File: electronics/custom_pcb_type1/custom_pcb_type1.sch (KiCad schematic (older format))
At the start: 24 parts, among them J1 BELT_CONN_1, J2 BELT_CONN_2, J3 SEN0140, Q1 2N2222, Q2 2N2222, Q3 2N2222, Q4 2N2222, Q5 2N2222, Q6 2N2222, SW1 RST_SW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

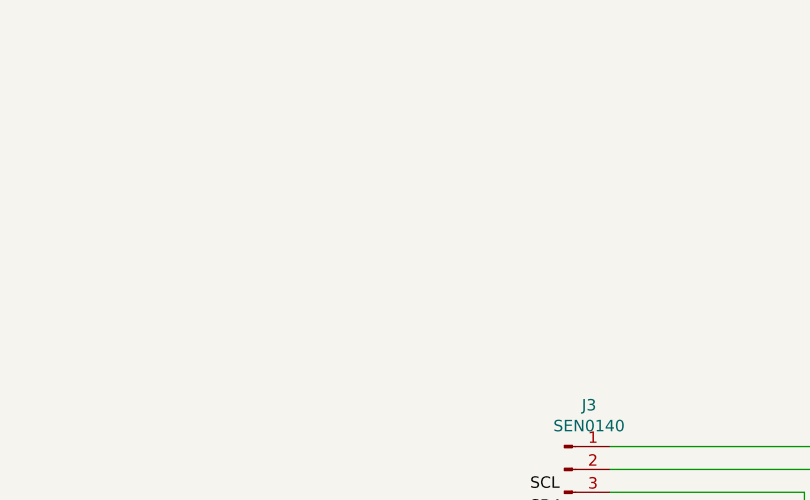
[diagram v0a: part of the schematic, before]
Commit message: Added USB connector
I'm pulling power from a secondary USB port on my prototype board and I plan to do the same here. The +5V from the USB port is used directly by everything and is passed to the atmega through its usb port.
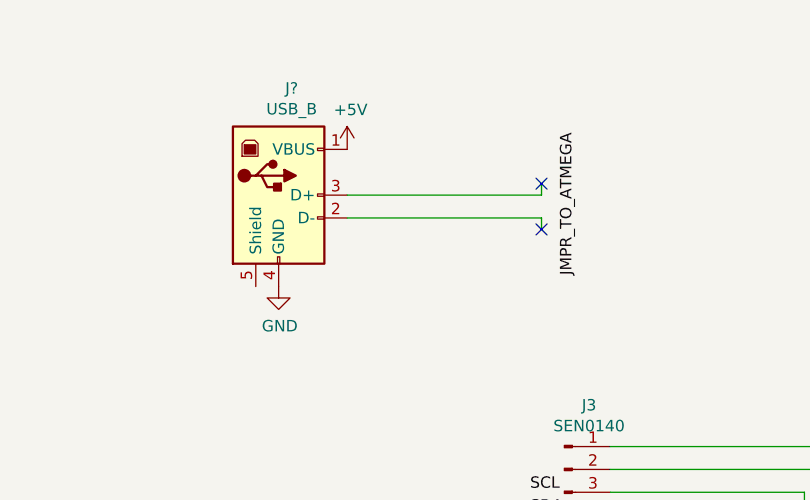
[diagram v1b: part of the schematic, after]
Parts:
- added J?: USB_B, symbol Connector:USB_B
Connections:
- net +5V: now also J?.1 (VBUS)
- net GND: now also J?.4 (GND)
- no-connect marks 0 -> 2
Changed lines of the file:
@@
 Wire Wire Line
 	5250 3150 5250 3600
+$Comp
+L Connector:USB_B J?
+U 1 1 609CD78C
+P 1150 1300
+F 0 "J?" H 1207 1767 50  0000 C CNN
+F 1 "USB_B" H 1207 1676 50  0000 C CNN
+F 2 "" H 1300 1250 50  0001 C CNN
+F 3 " ~" H 1300 1250 50  0001 C CNN
+	1    1150 1300
+	1    0    0    -1
+$EndComp
+$Comp
+L power:GND #PWR?
+U 1 1 609CF541
+P 1150 1700
+F 0 "#PWR?" H 1150 1450 50  0001 C CNN
+F 1 "GND" H 1155 1527 50  0000 C CNN
+F 2 "" H 1150 1700 50  0001 C CNN
+F 3 "" H 1150 1700 50  0001 C CNN
+	1    1150 1700
+	1    0    0    -1
+$EndComp
+$Comp
+L power:+5V #PWR?
+U 1 1 609D041E
+P 1450 1100
+F 0 "#PWR?" H 1450 950 50  0001 C CNN
+F 1 "+5V" H 1465 1273 50  0000 C CNN
+F 2 "" H 1450 1100 50  0001 C CNN
+F 3 "" H 1450 1100 50  0001 C CNN
+	1    1450 1100
+	1    0    0    -1
+$EndComp
+Wire Wire Line
+	2300 1300 2300 1250
+Wire Wire Line
+	1450 1300 2300 1300
+Wire Wire Line
+	1450 1400 2300 1400
+Wire Wire Line
+	2300 1400 2300 1450
+NoConn ~ 2300 1250
+NoConn ~ 2300 1450
+Text Label 2450 1650 1    50   ~ 0
+JMPR_TO_ATMEGA
 $EndSCHEMATC

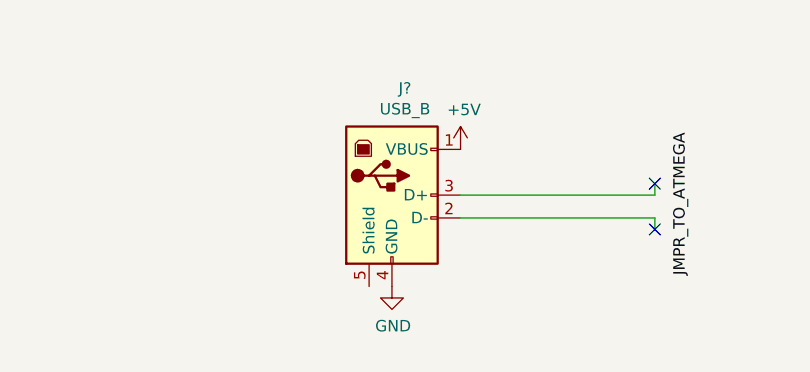
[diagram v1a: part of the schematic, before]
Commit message: Physical PCB start
Sort of got a start on the physical PCB layout. Its hard to lay things out in ways that don't overlap with other traces on a single layer. I got most of everything connected up and I think what I have left will need to be on the other side of the PCB. Will try and figure that out tomorrow.
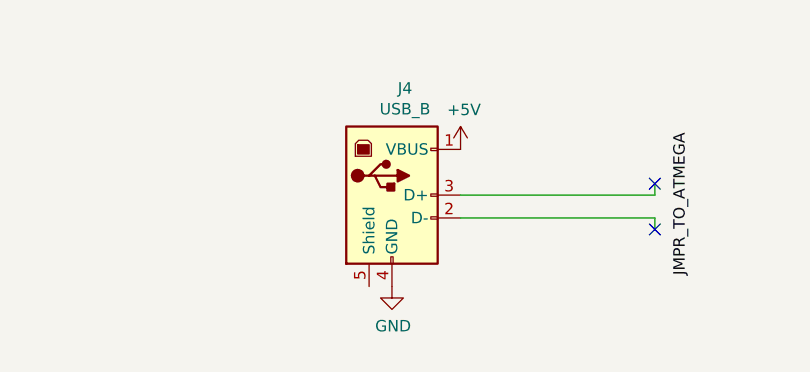
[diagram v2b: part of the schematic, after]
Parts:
- D1: footprint (none) -> LED_THT:LED_D5.0mm-4_RGB_Staggered_Pins
- J1, J2: footprint (none) -> Connector_PinHeader_2.54mm:PinHeader_2x03_P2.54mm_Horizontal
- J3: footprint (none) -> Connector_PinSocket_2.54mm:PinSocket_1x04_P2.54mm_Vertical
- J4: renamed from J?; footprint (none) -> Connector_USB:USB_B_OST_USB-B1HSxx_Horizontal
- R1, R2, R3, R4, R5, R6, R7, R8, R9: footprint (none) -> Resistor_THT:R_Axial_DIN0207_L6.3mm_D2.5mm_P10.16mm_Horizontal
- RV1, RV2, RV3: footprint (none) -> Potentiometer_THT:Potentiometer_Runtron_RM-065_Vertical
- SW1: footprint (none) -> Button_Switch_THT:SW_PUSH_6mm
- U1: footprint MODULE_MEGA_PRO_EMBED_CH340G_/_ATMEGA2560 -> MODULE_MEGA_PRO_EMBED_CH340G_:_ATMEGA2560
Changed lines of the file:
@@
 F 0 "U1" V 3204 1770 50  0000 R CNN
 F 1 "MEGA_PRO_EMBED_CH340G___ATMEGA2560" V 3295 1770 50  0000 R CNN
-F 2 "MODULE_MEGA_PRO_EMBED_CH340G_/_ATMEGA2560" H 3250 4300 50  0001 L BNN
+F 2 "MODULE_MEGA_PRO_EMBED_CH340G_:_ATMEGA2560" H 3250 4300 50  0001 L BNN
 F 3 "" H 3250 4300 50  0001 L BNN
 F 4 "" H 3250 4300 50  0001 L BNN "MAXIMUM_PACKAGE_HIEGHT"
@@
 F 0 "J2" H 10322 2424 50  0000 R CNN
 F 1 "BELT_CONN_2" H 10322 2333 50  0000 R CNN
-F 2 "" H 10350 2450 50  0001 C CNN
+F 2 "Connector_PinHeader_2.54mm:PinHeader_2x03_P2.54mm_Horizontal" H 10350 2450 50  0001 C CNN
 F 3 "~" H 10350 2450 50  0001 C CNN
 	1    10350 2450
@@
 F 0 "J1" H 10322 3624 50  0000 R CNN
 F 1 "BELT_CONN_1" H 10322 3533 50  0000 R CNN
-F 2 "" H 10350 3650 50  0001 C CNN
+F 2 "Connector_PinHeader_2.54mm:PinHeader_2x03_P2.54mm_Horizontal" H 10350 3650 50  0001 C CNN
 F 3 "~" H 10350 3650 50  0001 C CNN
 	1    10350 3650
@@
 F 0 "D1" H 1300 6497 50  0000 C CNN
 F 1 "LED_RGBC" H 1300 6406 50  0000 C CNN
-F 2 "" H 1300 5950 50  0001 C CNN
+F 2 "LED_THT:LED_D5.0mm-4_RGB_Staggered_Pins" H 1300 5950 50  0001 C CNN
 F 3 "~" H 1300 5950 50  0001 C CNN
 	1    1300 6000
@@
 F 0 "R4" V 5300 1100 50  0000 L CNN
 F 1 "1.8K" V 5400 1100 50  0000 L CNN
-F 2 "" H 5200 1150 50  0001 C CNN
+F 2 "Resistor_THT:R_Axial_DIN0207_L6.3mm_D2.5mm_P10.16mm_Horizontal" H 5200 1150 50  0001 C CNN
 F 3 "~" H 5200 1150 50  0001 C CNN
 	1    5200 1150
@@
 F 0 "R5" H 6368 1446 50  0000 L CNN
 F 1 "1.8K" H 6368 1355 50  0000 L CNN
-F 2 "" H 6300 1400 50  0001 C CNN
+F 2 "Resistor_THT:R_Axial_DIN0207_L6.3mm_D2.5mm_P10.16mm_Horizontal" H 6300 1400 50  0001 C CNN
 F 3 "~" H 6300 1400 50  0001 C CNN
 	1    6300 1400
@@
 F 0 "R6" H 7168 1446 50  0000 L CNN
 F 1 "1.8K" H 7168 1355 50  0000 L CNN
-F 2 "" H 7100 1400 50  0001 C CNN
+F 2 "Resistor_THT:R_Axial_DIN0207_L6.3mm_D2.5mm_P10.16mm_Horizontal" H 7100 1400 50  0001 C CNN
 F 3 "~" H 7100 1400 50  0001 C CNN
 	1    7100 1400
@@
 F 0 "R7" H 7968 1446 50  0000 L CNN
 F 1 "1.8K" H 7968 1355 50  0000 L CNN
-F 2 "" H 7900 1400 50  0001 C CNN
+F 2 "Resistor_THT:R_Axial_DIN0207_L6.3mm_D2.5mm_P10.16mm_Horizontal" H 7900 1400 50  0001 C CNN
 F 3 "~" H 7900 1400 50  0001 C CNN
 	1    7900 1400
@@
 F 0 "R8" H 8768 1446 50  0000 L CNN
 F 1 "1.8K" H 8768 1355 50  0000 L CNN
-F 2 "" H 8700 1400 50  0001 C CNN
+F 2 "Resistor_THT:R_Axial_DIN0207_L6.3mm_D2.5mm_P10.16mm_Horizontal" H 8700 1400 50  0001 C CNN
 F 3 "~" H 8700 1400 50  0001 C CNN
 	1    8700 1400
@@
 F 0 "R9" H 9568 1446 50  0000 L CNN
 F 1 "1.8K" H 9568 1355 50  0000 L CNN
-F 2 "" H 9500 1400 50  0001 C CNN
+F 2 "Resistor_THT:R_Axial_DIN0207_L6.3mm_D2.5mm_P10.16mm_Horizontal" H 9500 1400 50  0001 C CNN
 F 3 "~" H 9500 1400 50  0001 C CNN
 	1    9500 1400
@@
 F 0 "R1" H 1768 5546 50  0000 L CNN
 F 1 "330" H 1768 5455 50  0000 L CNN
-F 2 "" H 1700 5500 50  0001 C CNN
+F 2 "Resistor_THT:R_Axial_DIN0207_L6.3mm_D2.5mm_P10.16mm_Horizontal" H 1700 5500 50  0001 C CNN
 F 3 "~" H 1700 5500 50  0001 C CNN
 	1    1700 5500
@@
 F 0 "R2" H 2218 6096 50  0000 L CNN
 F 1 "330" H 2218 6005 50  0000 L CNN
-F 2 "" H 2150 6050 50  0001 C CNN
+F 2 "Resistor_THT:R_Axial_DIN0207_L6.3mm_D2.5mm_P10.16mm_Horizontal" H 2150 6050 50  0001 C CNN
 F 3 "~" H 2150 6050 50  0001 C CNN
 	1    2150 6050
@@
 F 0 "R3" H 2318 5296 50  0000 L CNN
 F 1 "330" H 2318 5205 50  0000 L CNN
-F 2 "" H 2250 5250 50  0001 C CNN
+F 2 "Resistor_THT:R_Axial_DIN0207_L6.3mm_D2.5mm_P10.16mm_Horizontal" H 2250 5250 50  0001 C CNN
 F 3 "~" H 2250 5250 50  0001 C CNN
 	1    2250 5250
@@
 F 0 "RV1" H 1833 7146 50  0000 R CNN
 F 1 "10K" H 1833 7055 50  0000 R CNN
-F 2 "" H 1900 7100 50  0001 C CNN
+F 2 "Potentiometer_THT:Potentiometer_Runtron_RM-065_Vertical" H 1900 7100 50  0001 C CNN
 F 3 "~" H 1900 7100 50  0001 C CNN
 	1    1900 7100
@@
 F 0 "RV2" H 2833 7146 50  0000 R CNN
 F 1 "10K" H 2833 7055 50  0000 R CNN
-F 2 "" H 2900 7100 50  0001 C CNN
+F 2 "Potentiometer_THT:Potentiometer_Runtron_RM-065_Vertical" H 2900 7100 50  0001 C CNN
 F 3 "~" H 2900 7100 50  0001 C CNN
 	1    2900 7100
@@
 F 0 "RV3" H 4033 7146 50  0000 R CNN
 F 1 "10K" H 4033 7055 50  0000 R CNN
-F 2 "" H 4100 7100 50  0001 C CNN
+F 2 "Potentiometer_THT:Potentiometer_Runtron_RM-065_Vertical" H 4100 7100 50  0001 C CNN
 F 3 "~" H 4100 7100 50  0001 C CNN
 	1    4100 7100
@@
 F 0 "J3" H 2508 2781 50  0000 C CNN
 F 1 "SEN0140" H 2508 2690 50  0000 C CNN
-F 2 "" H 2400 2500 50  0001 C CNN
+F 2 "Connector_PinSocket_2.54mm:PinSocket_1x04_P2.54mm_Vertical" H 2400 2500 50  0001 C CNN
 F 3 "~" H 2400 2500 50  0001 C CNN
 	1    2400 2500
@@
 F 0 "SW1" V 5296 2902 50  0000 R CNN
 F 1 "RST_SW" V 5205 2902 50  0000 R CNN
-F 2 "" H 5250 3150 50  0001 C CNN
+F 2 "Button_Switch_THT:SW_PUSH_6mm" H 5250 3150 50  0001 C CNN
 F 3 "http://www.apem.com/int/index.php?controller=attachment&id_attachment=488" H 5250 3150 50  0001 C CNN
 	1    5250 2950
@@
 	5250 3150 5250 3600
 $Comp
-L Connector:USB_B J?
+L Connector:USB_B J4
 U 1 1 609CD78C
 P 1150 1300
-F 0 "J?" H 1207 1767 50  0000 C CNN
+F 0 "J4" H 1207 1767 50  0000 C CNN
 F 1 "USB_B" H 1207 1676 50  0000 C CNN
-F 2 "" H 1300 1250 50  0001 C CNN
+F 2 "Connector_USB:USB_B_OST_USB-B1HSxx_Horizontal" H 1300 1250 50  0001 C CNN
 F 3 " ~" H 1300 1250 50  0001 C CNN
 	1    1150 1300
@@
 $EndComp
 $Comp
-L power:GND #PWR?
+L power:GND #PWR0111
 U 1 1 609CF541
 P 1150 1700
-F 0 "#PWR?" H 1150 1450 50  0001 C CNN
+F 0 "#PWR0111" H 1150 1450 50  0001 C CNN
 F 1 "GND" H 1155 1527 50  0000 C CNN
 F 2 "" H 1150 1700 50  0001 C CNN
@@
 $EndComp
 $Comp
-L power:+5V #PWR?
+L power:+5V #PWR0112
 U 1 1 609D041E
 P 1450 1100
-F 0 "#PWR?" H 1450 950 50  0001 C CNN
+F 0 "#PWR0112" H 1450 950 50  0001 C CNN
 F 1 "+5V" H 1465 1273 50  0000 C CNN
 F 2 "" H 1450 1100 50  0001 C CNN

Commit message: Better PCB routing
Before I started doing the back side routing I decided to try rerouting things for more traces on the top layer. I ended up changing the pinout to use even numbered pins 2-12 backwards (i.e. first motor is on pin 12, last motor on pin 2). That made routing SO much easier and I probably should have done that first. Now I think I'm down to just power and ground traces which I will have to do on the back for the most part. I know generally you're supposed to put data and power on the top layer and ground traces on the bottom but in this case just finishing it is all I want. Our bottom layer will be carefully placed ground and power traces unless we can finagle more room out of the top.
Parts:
- removed SW1: RST_SW, Button_Switch_THT:SW_PUSH_6mm, symbol Switch:SW_MEC_5G
- added SW1: RST_SW, Button_Switch_THT:SW_PUSH_6mm, symbol Switch:SW_Push
- D1: footprint LED_THT:LED_D5.0mm-4_RGB_Staggered_Pins -> LED_THT:LED_D5.0mm-4_RGB; symbol Device:LED_RGBC -> Device:LED_RGBC_GND2
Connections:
- net +5V: no longer J3.1 (Pin_1)
- net GND: now also D1.2 (K), SW1.1; no longer D1.4 (K), J3.2 (Pin_2)
- net at U1.5V_1 (5V), U1.5V_2 (5V), U1.5V_3 (5V): now also J3.1 (Pin_1)
- net at U1.D10: now also R5.2; no longer R9.2
- net at U1.D12: now also R4.2
- net at U1.D2: now also R9.2
- net at U1.D4: now also R8.2
- net at U1.D5: no longer R4.2
- net at U1.D6: now also R7.2; no longer R5.2
- net at U1.D7: no longer R6.2
- net at U1.D8: now also R6.2; no longer R7.2
- net at U1.D9: no longer R8.2
- net at U1.GND_1 (GND), U1.GND_2 (GND), U1.GND_3 (GND): now also J3.2 (Pin_2)
- net at U1.RST: now also SW1.2
- net at R1.2: now also D1.3 (GA); no longer D1.2 (GA)
- net at R2.2: now also D1.4 (BA); no longer D1.3 (BA)
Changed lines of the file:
@@
 	5500 1150 5300 1150
 Wire Wire Line
-	4250 1150 4250 3600
-Wire Wire Line
-	4150 5000 4150 5650
-Wire Wire Line
-	4150 5650 6300 5650
-Wire Wire Line
-	6300 5650 6300 1500
-Wire Wire Line
 	7100 1150 7100 1300
 Wire Wire Line
-	7100 1600 4150 1600
-Wire Wire Line
-	4150 1600 4150 3600
-Wire Wire Line
 	7900 1150 7900 1300
 Wire Wire Line
-	7900 5800 4050 5800
-Wire Wire Line
-	4050 5800 4050 5000
-Wire Wire Line
-	4050 3600 4050 1800
-Wire Wire Line
-	4050 1800 8700 1800
-Wire Wire Line
-	8700 1800 8700 1500
-Wire Wire Line
 	9500 1150 9500 1300
-Wire Wire Line
-	9500 5950 3950 5950
-Wire Wire Line
-	3950 5950 3950 5000
-$Comp
-L Device:LED_RGBC D1
-U 1 1 60A5A4AE
-P 1300 6000
-F 0 "D1" H 1300 6497 50  0000 C CNN
-F 1 "LED_RGBC" H 1300 6406 50  0000 C CNN
-F 2 "LED_THT:LED_D5.0mm-4_RGB_Staggered_Pins" H 1300 5950 50  0001 C CNN
-F 3 "~" H 1300 5950 50  0001 C CNN
-	1    1300 6000
-	1    0    0    -1
-$EndComp
 $Comp
 L power:GND #PWR0103
@@
 	0    1    1    0
 $EndComp
-Wire Wire Line
-	5100 1150 4250 1150
 $Comp
 L Device:R_Small_US R5
@@
 	1    0    0    -1
 $EndComp
-Wire Wire Line
-	7100 1500 7100 1600
 $Comp
 L Device:R_Small_US R7
@@
 	1    0    0    -1
 $EndComp
-Wire Wire Line
-	7900 1500 7900 5800
 $Comp
 L Device:R_Small_US R8
@@
 	1    0    0    -1
 $EndComp
-Wire Wire Line
-	9500 1500 9500 5950
 $Comp
 L Device:R_Small_US R1
@@
 	1    0    0    -1
 $EndComp
-$Comp
-L power:GND #PWR0108
-U 1 1 60AD6507
-P 3650 2500
-F 0 "#PWR0108" H 3650 2250 50  0001 C CNN
-F 1 "GND" H 3655 2327 50  0000 C CNN
-F 2 "" H 3650 2500 50  0001 C CNN
-F 3 "" H 3650 2500 50  0001 C CNN
-	1    3650 2500
-	1    0    0    -1
-$EndComp
-Wire Wire Line
-	2600 2500 3650 2500
-Wire Wire Line
-	2600 2600 3450 2600
-Wire Wire Line
-	3450 2600 3450 3600
-Wire Wire Line
-	2600 2700 6150 2700
 Wire Wire Line
 	6150 2700 6150 5250
@@
 Text Label 2250 2600 0    50   ~ 0
 SCL
-$Comp
-L power:+5V #PWR0109
-U 1 1 60AFB188
-P 3650 2400
-F 0 "#PWR0109" H 3650 2250 50  0001 C CNN
-F 1 "+5V" H 3665 2573 50  0000 C CNN
-F 2 "" H 3650 2400 50  0001 C CNN
-F 3 "" H 3650 2400 50  0001 C CNN
-	1    3650 2400
-	1    0    0    -1
-$EndComp
-Wire Wire Line
-	3650 2400 2600 2400
-$Comp
-L Switch:SW_MEC_5G SW1
-U 1 1 60B02D94
-P 5250 2950
-F 0 "SW1" V 5296 2902 50  0000 R CNN
-F 1 "RST_SW" V 5205 2902 50  0000 R CNN
-F 2 "Button_Switch_THT:SW_PUSH_6mm" H 5250 3150 50  0001 C CNN
-F 3 "http://www.apem.com/int/index.php?controller=attachment&id_attachment=488" H 5250 3150 50  0001 C CNN
-	1    5250 2950
-	0    -1   -1   0
-$EndComp
-$Comp
-L power:GND #PWR0110
-U 1 1 60B063B5
-P 5250 2750
-F 0 "#PWR0110" H 5250 2500 50  0001 C CNN
-F 1 "GND" H 5255 2577 50  0000 C CNN
-F 2 "" H 5250 2750 50  0001 C CNN
-F 3 "" H 5250 2750 50  0001 C CNN
-	1    5250 2750
-	1    0    0    1
-$EndComp
-Wire Wire Line
-	5250 3150 5250 3600
 $Comp
 L Connector:USB_B J4
@@
 Text Label 2450 1650 1    50   ~ 0
 JMPR_TO_ATMEGA
+$Comp
+L power:GND #PWR01
+U 1 1 609EAE83
+P 5250 2950
+F 0 "#PWR01" H 5250 2700 50  0001 C CNN
+F 1 "GND" H 5255 2777 50  0000 C CNN
+F 2 "" H 5250 2950 50  0001 C CNN
+F 3 "" H 5250 2950 50  0001 C CNN
+	1    5250 2950
+	-1   0    0    1
+$EndComp
+Wire Wire Line
+	5250 2950 5250 3050
+Wire Wire Line
+	5250 3450 5250 3600
+$Comp
+L Switch:SW_Push SW1
+U 1 1 60A27432
+P 5250 3250
+F 0 "SW1" V 5204 3398 50  0000 L CNN
+F 1 "RST_SW" V 5295 3398 50  0000 L CNN
+F 2 "Button_Switch_THT:SW_PUSH_6mm" H 5250 3450 50  0001 C CNN
+F 3 "~" H 5250 3450 50  0001 C CNN
+	1    5250 3250
+	0    1    1    0
+$EndComp
+$Comp
+L Device:LED_RGBC_GND2 D1
+U 1 1 60A5A4AE
+P 1300 6000
+F 0 "D1" H 1300 6497 50  0000 C CNN
+F 1 "LED_RGBC" H 1300 6406 50  0000 C CNN
+F 2 "LED_THT:LED_D5.0mm-4_RGB" H 1300 5950 50  0001 C CNN
+F 3 "~" H 1300 5950 50  0001 C CNN
+	1    1300 6000
+	1    0    0    -1
+$EndComp
+Wire Wire Line
+	9500 1500 9500 5050
+Wire Wire Line
+	9500 5050 4350 5050
+Wire Wire Line
+	4350 5050 4350 5000
+Wire Wire Line
+	4250 5000 4300 5000
+Wire Wire Line
+	4300 5000 4300 4950
+Wire Wire Line
+	4300 4950 8700 4950
+Wire Wire Line
+	8700 4950 8700 1500
+Wire Wire Line
+	7900 1500 7900 5100
+Wire Wire Line
+	7900 5100 4150 5100
+Wire Wire Line
+	4150 5100 4150 5000
+Wire Wire Line
+	4050 5000 4050 5150
+Wire Wire Line
+	4050 5150 7100 5150
+Wire Wire Line
+	7100 5150 7100 1500
+Wire Wire Line
+	6300 1500 6300 5350
+Wire Wire Line
+	6300 5350 3950 5350
+Wire Wire Line
+	3950 5350 3950 5000
+Wire Wire Line
+	3850 5000 3850 5500
+Wire Wire Line
+	3850 5500 5100 5500
+Wire Wire Line
+	5100 5500 5100 1150
+Wire Wire Line
+	2600 2700 6150 2700
+Wire Wire Line
+	3450 2600 3450 3600
+Wire Wire Line
+	2600 2600 3450 2600
+Wire Wire Line
+	2600 2400 5600 2400
+Wire Wire Line
+	5600 2400 5600 5000
+Wire Wire Line
+	5600 5000 5550 5000
+Wire Wire Line
+	2600 2500 900  2500
+Wire Wire Line
+	900  2500 900  5000
+Wire Wire Line
+	900  5000 850  5000
 $EndSCHEMATC

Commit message: PCB version 1.0
Ok I've finished laying everything out. In the end I was successful in laying out the data and power traces on top and only have ground traces on the bottom. I've generated the reversed masks that are ready for laser printing. Now I'm realizing that transferring the mask to the PCB is going to be a slightly involved task. I've settled on the rolling pin + hotplate method since I don't want to build a jig to hold an iron upside down and I don't want to spend the time modifying a cheap ebay laminator to work with PCBs. Going forward I may switch to a photoetching process instead since that doesn't require heat+pressure. Although it requires a few more chemicals it seems like a more controllable process. I did price out an online mfg and it was around $50 shipped for 5 boards. I'd be amazed if the first version of this board actually even works but maybe a future version I will order online instead.

Also something happened with the symbol library for the project and it generated a rescue lib. No idea why but it seems fine.
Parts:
- added J5: JMPR_TO_ATMEGA, Connector_PinHeader_2.54mm:PinHeader_1x02_P2.54mm_Horizontal, symbol Connector:Conn_01x02_Male
- D1: symbol Device:LED_RGBC_GND2 -> custom_pcb_type1-rescue:LED_RGBC_GND2-Device
- Q1, Q2, Q3, Q4, Q5, Q6: symbol Transistor_BJT:2N2222 -> custom_pcb_type1-rescue:2N2222-Transistor_BJT
- U1: symbol MEGA_PRO_EMBED_CH340G___ATMEGA2560:MEGA_PRO_EMBED_CH340G___ATMEGA2560 -> custom_pcb_type1-rescue:MEGA_PRO_EMBED_CH340G___ATMEGA2560-MEGA_PRO_EMBED_CH340G___ATMEGA2560
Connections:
- net labels removed: JMPR_TO_ATMEGA
- wire segments 93 -> 91
- no-connect marks 2 -> 0
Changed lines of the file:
@@
 $EndDescr
 $Comp
-L Transistor_BJT:2N2222 Q2
+L custom_pcb_type1-rescue:2N2222-Transistor_BJT Q2
 U 1 1 609EAC55
 P 6500 1150
@@
 $EndComp
 $Comp
-L Transistor_BJT:2N2222 Q3
+L custom_pcb_type1-rescue:2N2222-Transistor_BJT Q3
 U 1 1 609EB0CD
 P 7300 1150
@@
 $EndComp
 $Comp
-L Transistor_BJT:2N2222 Q4
+L custom_pcb_type1-rescue:2N2222-Transistor_BJT Q4
 U 1 1 609EBA66
 P 8100 1150
@@
 $EndComp
 $Comp
-L MEGA_PRO_EMBED_CH340G___ATMEGA2560:MEGA_PRO_EMBED_CH340G___ATMEGA2560 U1
+L custom_pcb_type1-rescue:MEGA_PRO_EMBED_CH340G___ATMEGA2560-MEGA_PRO_EMBED_CH340G___ATMEGA2560 U1
 U 1 1 609C607E
 P 3250 4300
@@
 $EndComp
 $Comp
-L Transistor_BJT:2N2222 Q5
+L custom_pcb_type1-rescue:2N2222-Transistor_BJT Q5
 U 1 1 609ECC79
 P 8900 1150
@@
 $EndComp
 $Comp
-L Transistor_BJT:2N2222 Q6
+L custom_pcb_type1-rescue:2N2222-Transistor_BJT Q6
 U 1 1 609F368F
 P 9700 1150
@@
 $EndComp
 $Comp
-L Transistor_BJT:2N2222 Q1
+L custom_pcb_type1-rescue:2N2222-Transistor_BJT Q1
 U 1 1 609EA32B
 P 5700 1150
@@
 $EndComp
 Wire Wire Line
-	2300 1300 2300 1250
-Wire Wire Line
 	1450 1300 2300 1300
 Wire Wire Line
 	1450 1400 2300 1400
-Wire Wire Line
-	2300 1400 2300 1450
-NoConn ~ 2300 1250
-NoConn ~ 2300 1450
-Text Label 2450 1650 1    50   ~ 0
-JMPR_TO_ATMEGA
 $Comp
 L power:GND #PWR01
@@
 $EndComp
 $Comp
-L Device:LED_RGBC_GND2 D1
+L custom_pcb_type1-rescue:LED_RGBC_GND2-Device D1
 U 1 1 60A5A4AE
 P 1300 6000
@@
 Wire Wire Line
 	900  5000 850  5000
+$Comp
+L Connector:Conn_01x02_Male J5
+U 1 1 60A08FAC
+P 2500 1400
+F 0 "J5" H 2472 1282 50  0000 R CNN
+F 1 "JMPR_TO_ATMEGA" H 2472 1373 50  0000 R CNN
+F 2 "Connector_PinHeader_2.54mm:PinHeader_1x02_P2.54mm_Horizontal" H 2500 1400 50  0001 C CNN
+F 3 "~" H 2500 1400 50  0001 C CNN
+	1    2500 1400
+	-1   0    0    1
+$EndComp
 $EndSCHEMATC

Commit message: Size matters
Welp Got all the way to putting the transfer paper onto the PCB when I found out that my raw PCBs are kinda small. 70mm x 100mm - which is a lot smaller than the current footprint of like 90mm x 120mm. So LOTS of rearranging things and reassigning pins. I think the end result is a far better board than the previous one so It was well worth the effort. I made sure to not route any traces too close to the edge, other traces, or other pin holes. Trying to give the toner transfer the best possible chance of at least not bridging stuff.
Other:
- moved on the sheet: R2
